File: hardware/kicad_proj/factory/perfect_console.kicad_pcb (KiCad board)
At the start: 2 copper layers, 70 x 60 mm, 66 parts, among them J1 USB, J10 I2C, J11 ESP_UART, J12 CH_UART, J13 CH_Flash, J14 Micro_SD_Card, J16 DISP_MISO, J2 TP4056_WO_Protect, J3 Bat, J4 PWR_Btn, J5 BTNS, J6 PTT_Btn, J7 PWR_OUT, J8 40-41, J9 USB_Data, Q1 NMOS, Q2 NMOS, Q3 NMOS, Q4 NMOS, Q5 NMOS, Q6 NMOS, SW1 Reset, SW2 Boot, U1 ESP32-S3-WROOM1, U2 Display, U3 PCM5102, U4 CH32V006E8R6, U5 LoRa, U6 USBLC6-2SC6, U7 Mic, U8 DC-DC

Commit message: Покращення PCB
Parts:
- added C13: 10uF, Capacitor_SMD:C_1206_3216Metric_Pad1.33x1.80mm_HandSolder, F.Cu at (265.2, 205.2)
- C1, C10, C11, C12, C2, C3, C6, C7, C8, C9: footprint Capacitor_SMD:C_1206_3216Metric -> Capacitor_SMD:C_1206_3216Metric_Pad1.33x1.80mm_HandSolder
- C4: value 20uF -> 10uF; footprint Capacitor_SMD:C_1206_3216Metric -> Capacitor_SMD:C_1206_3216Metric_Pad1.33x1.80mm_HandSolder
- C5: value 0.1uF -> 100nF; footprint Capacitor_SMD:C_1206_3216Metric -> Capacitor_SMD:C_1206_3216Metric_Pad1.33x1.80mm_HandSolder
- moved C4 1.49 mm to (262.4, 208.1)
- moved C3 0.58 mm to (284.4, 210.3)
- moved C8 0.18 mm to (271.8, 231.2)
- moved C11 0.12 mm to (303.8, 198.1)
- moved C12 0.12 mm to (303.8, 195.2)
- moved C10 0.12 mm to (287.8, 228.1)
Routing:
- net MIC_PWR: track 37.1 -> 31.5 mm, vias 0 -> 2
- net Net-(Q3-D): track 16.7 -> 17.9 mm
- net GND1: track 96.6 -> 97.1 mm
- net GND: track 186.6 -> 186.1 mm
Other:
- board text added: "v1.1 by Kolodieiev"
- board text removed: "v1.0 by Kolodieiev"

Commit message: Видалено ESD мікросхему та її конденсатор
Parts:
- removed C7: 100nF, Capacitor_SMD:C_1206_3216Metric_Pad1.33x1.80mm_HandSolder
- removed U6: USBLC6-2SC6, Package_TO_SOT_SMD:SOT-23-6
- moved C5 1.77 mm to (272.4, 202.5)
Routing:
- net GND: track 186.1 -> 168.4 mm, vias 2 -> 1
- net VBUS: track 44.3 -> 30.9 mm, vias 1 -> 0
- net DISP_RST: track 29.4 -> 28.4 mm
- net DISP_D/C: track 28.6 -> 27.6 mm
- net MIC_PWR: track 31.5 -> 32.3 mm, vias 2 -> 0
- net Net-(Q3-D): track 17.9 -> 17.3 mm
- net +4V2: track 129.4 -> 128.8 mm

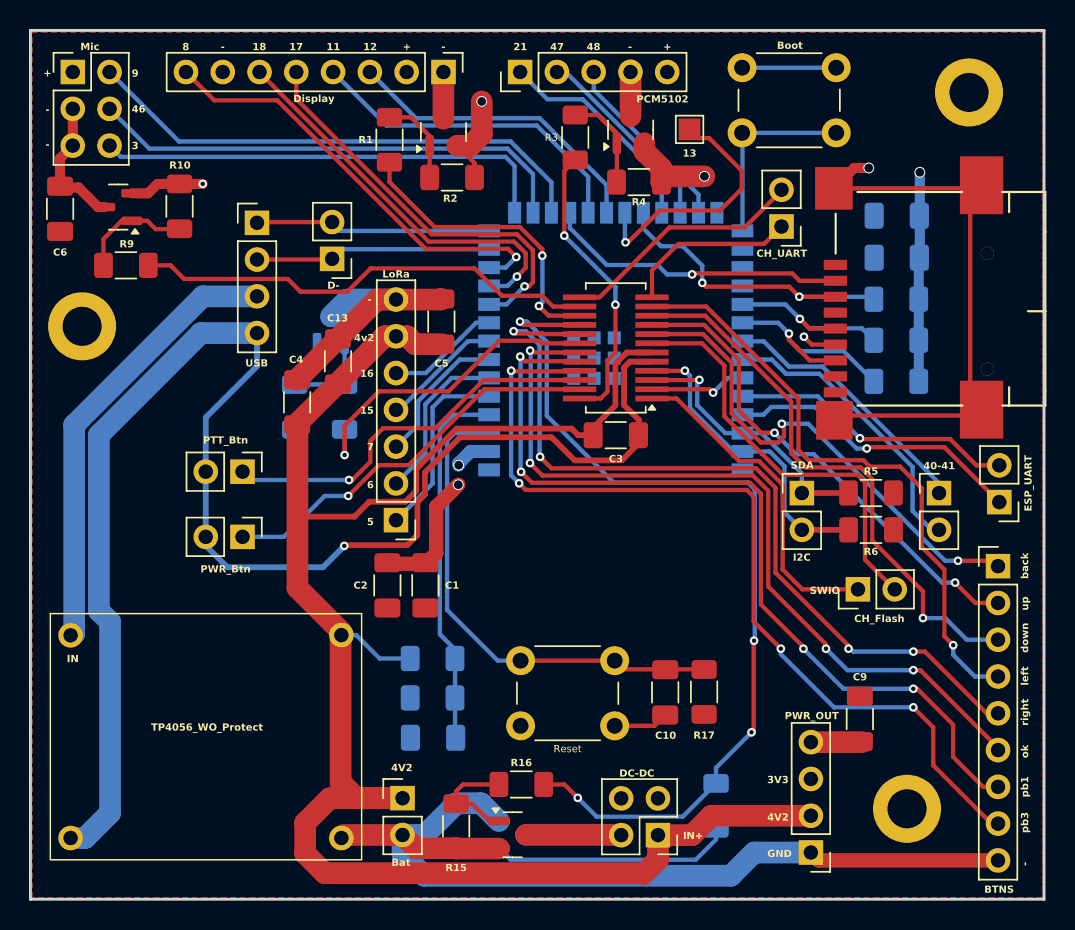
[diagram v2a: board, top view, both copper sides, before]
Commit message: Зменшено розміри плати
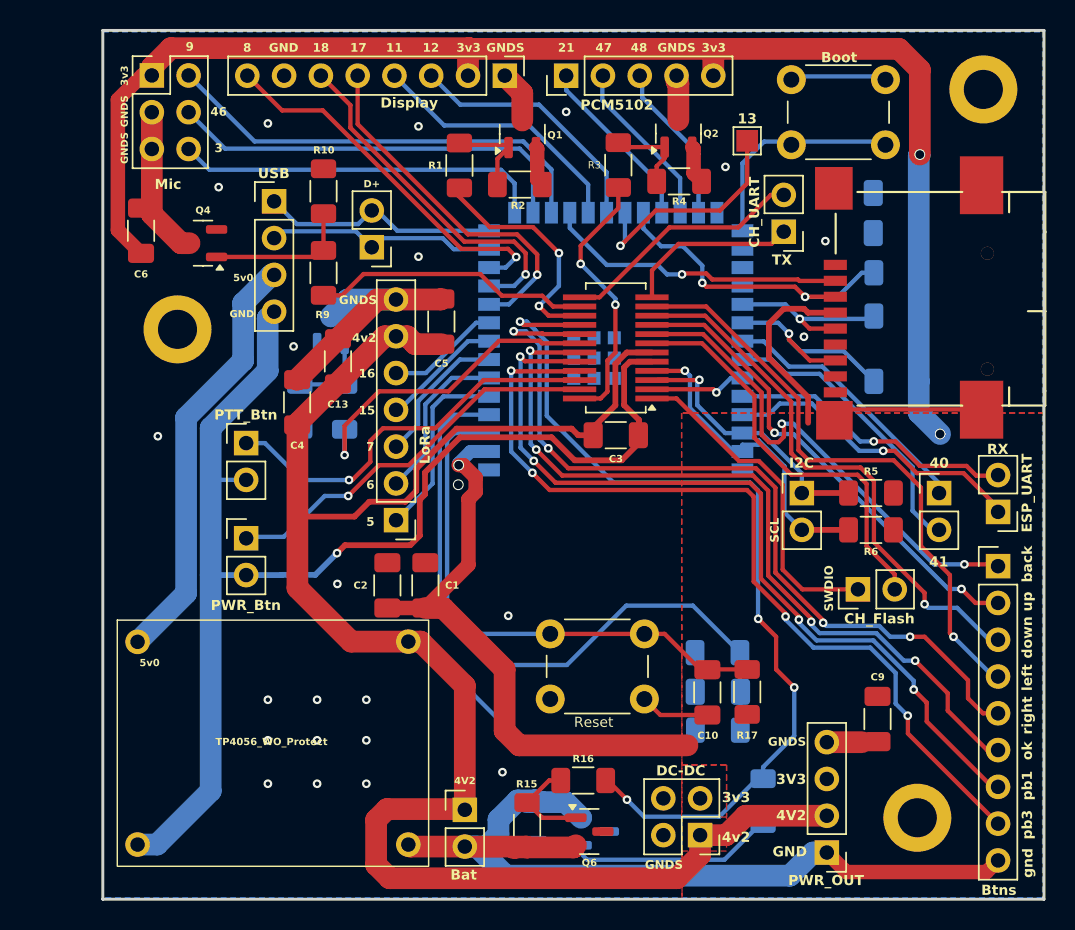
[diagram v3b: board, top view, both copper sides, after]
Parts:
- J8: value 40-41 -> 40
- Q1, Q2, Q3, Q4, Q5, Q6: value NMOS -> A09T
- moved R11 20.3 mm to (291.5, 230.7)
- moved C8 19.9 mm to (291.5, 228.1)
- moved R12 19.9 mm to (291.4, 225.3)
- moved R9 13.7 mm to (264.2, 199.1), turned to 90 degrees
- moved R10 9.99 mm to (264.2, 193.5)
- moved H2 6.59 mm to (254.2, 203.0)
- moved Q4 6.36 mm to (255.9, 197.1)
- moved C6 5.79 mm to (251.6, 196.2)
- moved Q5 5.69 mm to (283.0, 237.7)
- moved U7 5.47 mm to (252.4, 185.5)
- moved R13 5.45 mm to (278.9, 237.1)
- moved Q1 5.45 mm to (278.0, 189.5)
- moved Q6 5.30 mm to (282.6, 237.7)
- moved R1 5.14 mm to (273.6, 191.7)
- moved R15 4.90 mm to (278.3, 237.2)
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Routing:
- net +3V3: track 17.0 -> 153.5 mm, vias 2 -> 3
- net GND1: track 97.1 -> 32.9 mm, vias 6 -> 23
- net VVAL: track 26.3 -> 47.0 mm
- net +4V2: track 128.8 -> 145.7 mm
- net GND: track 168.4 -> 152.3 mm
- net MIC_PWR: track 32.3 -> 19.2 mm
- net MIC_SCK: track 31.8 -> 25.5 mm
- net MIC_WS: track 33.8 -> 28.7 mm
- net MIC_SD: track 35.8 -> 30.7 mm
- net DISP_MOSI: track 23.1 -> 18.4 mm
- net DISP_PWR: track 20.9 -> 16.4 mm
- net DISP_BLK: track 30.3 -> 25.9 mm
- net DISP_SCK: track 21.5 -> 17.7 mm
- net DISP_RST: track 28.4 -> 25.1 mm
- net DISP_D/C: track 27.6 -> 24.5 mm
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- added copper zone on F.Cu, net GND1
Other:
- board size 70 x 60 mm -> 65 x 60 mm
- board text added: "3v3"
- board text added: "41"
- board text added: "5v0"
- board text added: "Btns"
- board text added: "D+"
- board text added: "GNDS"
- board text added: "RX"
- board text added: "SCL"
- board text added: "SWDIO"
- board text added: "TX"
- board text added: "gnd"
- board text added: "v1.2 by Kolodieiev"
- board text removed: "+"
- board text removed: "-"
- board text removed: "BTNS"
- board text removed: "D-"
- board text removed: "IN"
- board text removed: "IN+"
- board text removed: "SDA"
- board text removed: "SWIO"
- board text removed: "v1.1 by Kolodieiev"
